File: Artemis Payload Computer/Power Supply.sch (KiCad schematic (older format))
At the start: 3 parts, among them U501 MIC39100-5.0WS

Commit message: complete redo hehe
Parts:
- renumbered C502 to C?, C501 to C?, U501 to U?
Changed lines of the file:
@@
 $Descr A4 11693 8268
 encoding utf-8
-Sheet 5 5
+Sheet 6 6
 Title ""
 Date ""
@@
 $EndDescr
 $Comp
-L MIC39100-5.0WS:MIC39100-5.0WS U501
+L MIC39100-5.0WS:MIC39100-5.0WS U?
 U 1 1 603A9BB7
 P 6150 3400
-F 0 "U501" H 6150 3667 50  0000 C CNN
+F 0 "U?" H 6150 3667 50  0000 C CNN
 F 1 "MIC39100-5.0WS" H 6150 3576 50  0000 C CNN
 F 2 "SOT223" H 6150 3400 50  0001 L BNN
@@
 $EndComp
 $Comp
-L power:+BATT #PWR0101
+L power:+BATT #PWR?
 U 1 1 603AA4B7
 P 5450 3400
-F 0 "#PWR0101" H 5450 3250 50  0001 C CNN
+F 0 "#PWR?" H 5450 3250 50  0001 C CNN
 F 1 "+BATT" V 5465 3527 50  0000 L CNN
 F 2 "" H 5450 3400 50  0001 C CNN
@@
 $EndComp
 $Comp
-L power:+5V #PWR0102
+L power:+5V #PWR?
 U 1 1 603AAE10
 P 6900 3400
-F 0 "#PWR0102" H 6900 3250 50  0001 C CNN
+F 0 "#PWR?" H 6900 3250 50  0001 C CNN
 F 1 "+5V" V 6915 3528 50  0000 L CNN
 F 2 "" H 6900 3400 50  0001 C CNN
@@
 	6550 3400 6750 3400
 $Comp
-L power:GND #PWR0103
+L power:GND #PWR?
 U 1 1 603ABA0D
 P 6050 3900
-F 0 "#PWR0103" H 6050 3650 50  0001 C CNN
+F 0 "#PWR?" H 6050 3650 50  0001 C CNN
 F 1 "GND" H 6055 3727 50  0000 C CNN
 F 2 "" H 6050 3900 50  0001 C CNN
@@
 	6050 3800 6050 3900
 $Comp
-L Device:C C502
+L Device:C C?
 U 1 1 603ABFDD
 P 6750 3550
-F 0 "C502" H 6865 3596 50  0000 L CNN
+F 0 "C?" H 6865 3596 50  0000 L CNN
 F 1 "10 uF" H 6865 3505 50  0000 L CNN
 F 2 "Capacitor_SMD:C_0603_1608Metric_Pad1.08x0.95mm_HandSolder" H 6788 3400 50  0001 C CNN
@@
 	5450 3400 5500 3400
 $Comp
-L Device:C C501
+L Device:C C?
 U 1 1 603ACE4A
 P 5500 3550
-F 0 "C501" H 5615 3596 50  0000 L CNN
+F 0 "C?" H 5615 3596 50  0000 L CNN
 F 1 "10 uF" H 5615 3505 50  0000 L CNN
 F 2 "Capacitor_SMD:C_0603_1608Metric_Pad1.08x0.95mm_HandSolder" H 5538 3400 50  0001 C CNN

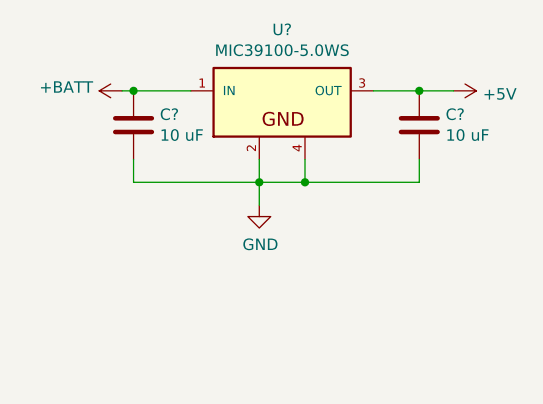
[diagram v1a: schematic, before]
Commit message: Updated Footprints
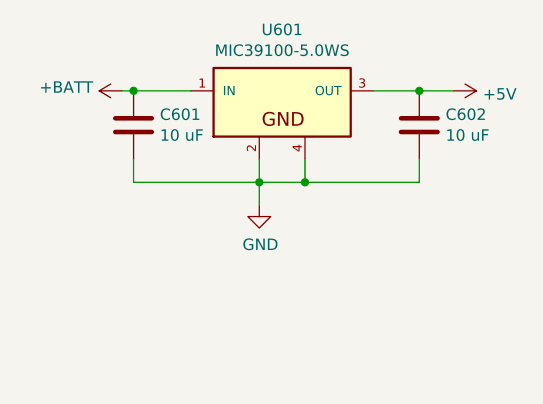
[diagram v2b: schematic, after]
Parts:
- U601: renamed from U?; footprint SOT223 -> Package_TO_SOT_SMD:SOT-223
- gave numbers to parts that had none: 2
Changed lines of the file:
@@
 $EndDescr
 $Comp
-L MIC39100-5.0WS:MIC39100-5.0WS U?
+L MIC39100-5.0WS:MIC39100-5.0WS U601
 U 1 1 603A9BB7
 P 6150 3400
-F 0 "U?" H 6150 3667 50  0000 C CNN
+F 0 "U601" H 6150 3667 50  0000 C CNN
 F 1 "MIC39100-5.0WS" H 6150 3576 50  0000 C CNN
-F 2 "SOT223" H 6150 3400 50  0001 L BNN
+F 2 "Package_TO_SOT_SMD:SOT-223" H 6150 3400 50  0001 L BNN
 F 3 "https://ww1.microchip.com/downloads/en/DeviceDoc/20005834A.pdf" H 6150 3400 50  0001 L BNN
 F 4 "" H 6150 3400 50  0001 L BNN "PARTNUM"
@@
 $EndComp
 $Comp
-L power:+BATT #PWR?
+L power:+BATT #PWR0103
 U 1 1 603AA4B7
 P 5450 3400
-F 0 "#PWR?" H 5450 3250 50  0001 C CNN
+F 0 "#PWR0103" H 5450 3250 50  0001 C CNN
 F 1 "+BATT" V 5465 3527 50  0000 L CNN
 F 2 "" H 5450 3400 50  0001 C CNN
@@
 $EndComp
 $Comp
-L power:+5V #PWR?
+L power:+5V #PWR0104
 U 1 1 603AAE10
 P 6900 3400
-F 0 "#PWR?" H 6900 3250 50  0001 C CNN
+F 0 "#PWR0104" H 6900 3250 50  0001 C CNN
 F 1 "+5V" V 6915 3528 50  0000 L CNN
 F 2 "" H 6900 3400 50  0001 C CNN
@@
 	6550 3400 6750 3400
 $Comp
-L power:GND #PWR?
+L power:GND #PWR0105
 U 1 1 603ABA0D
 P 6050 3900
-F 0 "#PWR?" H 6050 3650 50  0001 C CNN
+F 0 "#PWR0105" H 6050 3650 50  0001 C CNN
 F 1 "GND" H 6055 3727 50  0000 C CNN
 F 2 "" H 6050 3900 50  0001 C CNN
@@
 	6050 3800 6050 3900
 $Comp
-L Device:C C?
+L Device:C C602
 U 1 1 603ABFDD
 P 6750 3550
-F 0 "C?" H 6865 3596 50  0000 L CNN
+F 0 "C602" H 6865 3596 50  0000 L CNN
 F 1 "10 uF" H 6865 3505 50  0000 L CNN
 F 2 "Capacitor_SMD:C_0603_1608Metric_Pad1.08x0.95mm_HandSolder" H 6788 3400 50  0001 C CNN
@@
 	5450 3400 5500 3400
 $Comp
-L Device:C C?
+L Device:C C601
 U 1 1 603ACE4A
 P 5500 3550
-F 0 "C?" H 5615 3596 50  0000 L CNN
+F 0 "C601" H 5615 3596 50  0000 L CNN
 F 1 "10 uF" H 5615 3505 50  0000 L CNN
 F 2 "Capacitor_SMD:C_0603_1608Metric_Pad1.08x0.95mm_HandSolder" H 5538 3400 50  0001 C CNN

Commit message: ready for testing...
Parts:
- added J601: Connector_Screw_Terminal_01x02, TerminalBlock:TerminalBlock_bornier-2_P5.08mm, symbol Artemis_Payload_Computer-cache:Connector_Screw_Terminal_01x02
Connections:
- net +BATT: now also J601.2 (Pin_2)
- net GND: now also J601.1 (Pin_1)
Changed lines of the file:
@@
 Wire Wire Line
 	5500 3800 5500 3700
+$Comp
+L Artemis_Payload_Computer-cache:Connector_Screw_Terminal_01x02 J601
+U 1 1 60408505
+P 5650 4450
+F 0 "J601" H 5568 4125 50  0000 C CNN
+F 1 "Connector_Screw_Terminal_01x02" H 5568 4216 50  0000 C CNN
+F 2 "TerminalBlock:TerminalBlock_bornier-2_P5.08mm" H 5650 4450 50  0001 C CNN
+F 3 "" H 5650 4450 50  0001 C CNN
+	1    5650 4450
+	-1   0    0    1
+$EndComp
+$Comp
+L power:+BATT #PWR0113
+U 1 1 60408CE9
+P 6400 4350
+F 0 "#PWR0113" H 6400 4200 50  0001 C CNN
+F 1 "+BATT" V 6415 4477 50  0000 L CNN
+F 2 "" H 6400 4350 50  0001 C CNN
+F 3 "" H 6400 4350 50  0001 C CNN
+	1    6400 4350
+	0    1    1    0
+$EndComp
+$Comp
+L power:GND #PWR0114
+U 1 1 60409215
+P 6400 4600
+F 0 "#PWR0114" H 6400 4350 50  0001 C CNN
+F 1 "GND" H 6405 4427 50  0000 C CNN
+F 2 "" H 6400 4600 50  0001 C CNN
+F 3 "" H 6400 4600 50  0001 C CNN
+	1    6400 4600
+	0    -1   -1   0
+$EndComp
+Wire Wire Line
+	5850 4350 6400 4350
+Wire Wire Line
+	5850 4450 6150 4450
+Wire Wire Line
+	6150 4450 6150 4600
+Wire Wire Line
+	6150 4600 6400 4600
 $EndSCHEMATC

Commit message: Minor Changes. Approved for ordering
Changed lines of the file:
@@
 Wire Wire Line
 	6050 3700 6050 3800
-Wire Wire Line
-	6250 3700 6250 3800
-Wire Wire Line
-	6250 3800 6050 3800
 Connection ~ 6050 3800
 Wire Wire Line
@@
 Wire Wire Line
 	6750 3700 6750 3800
-Wire Wire Line
-	6750 3800 6250 3800
-Connection ~ 6250 3800
 Wire Wire Line
 	5450 3400 5500 3400
@@
 Wire Wire Line
 	6150 4600 6400 4600
+Wire Wire Line
+	6050 3800 6250 3800
+Wire Wire Line
+	6250 3700 6250 3800
+Connection ~ 6250 3800
+Wire Wire Line
+	6250 3800 6750 3800
 $EndSCHEMATC
